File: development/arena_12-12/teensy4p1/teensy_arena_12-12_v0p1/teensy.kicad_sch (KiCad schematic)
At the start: 3 parts, among them J2 Conn_01x04, J3 Conn_01x04, U18 Teensy4.1

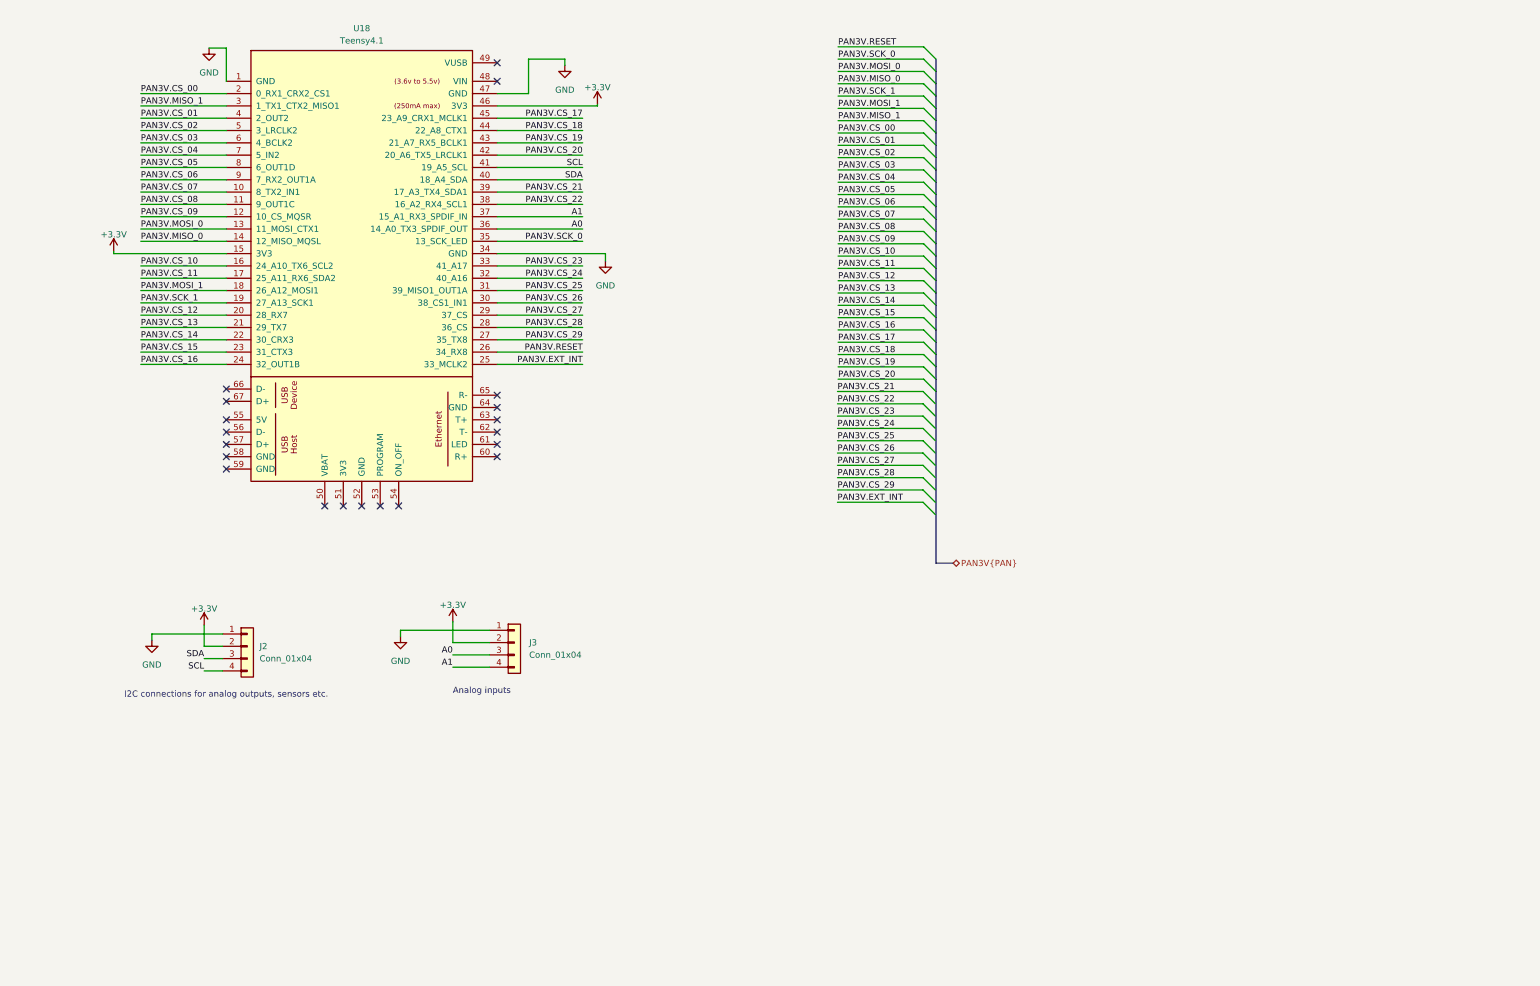
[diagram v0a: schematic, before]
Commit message: Worked on 12-12 teensy4p1 arena without vreg.
Modified SPI connections from teensy to panel columns so that all
signals go from a single source to a single destinatin. Also, added
source termination resistors and schmitt trigger buffers to all SPI
signals.
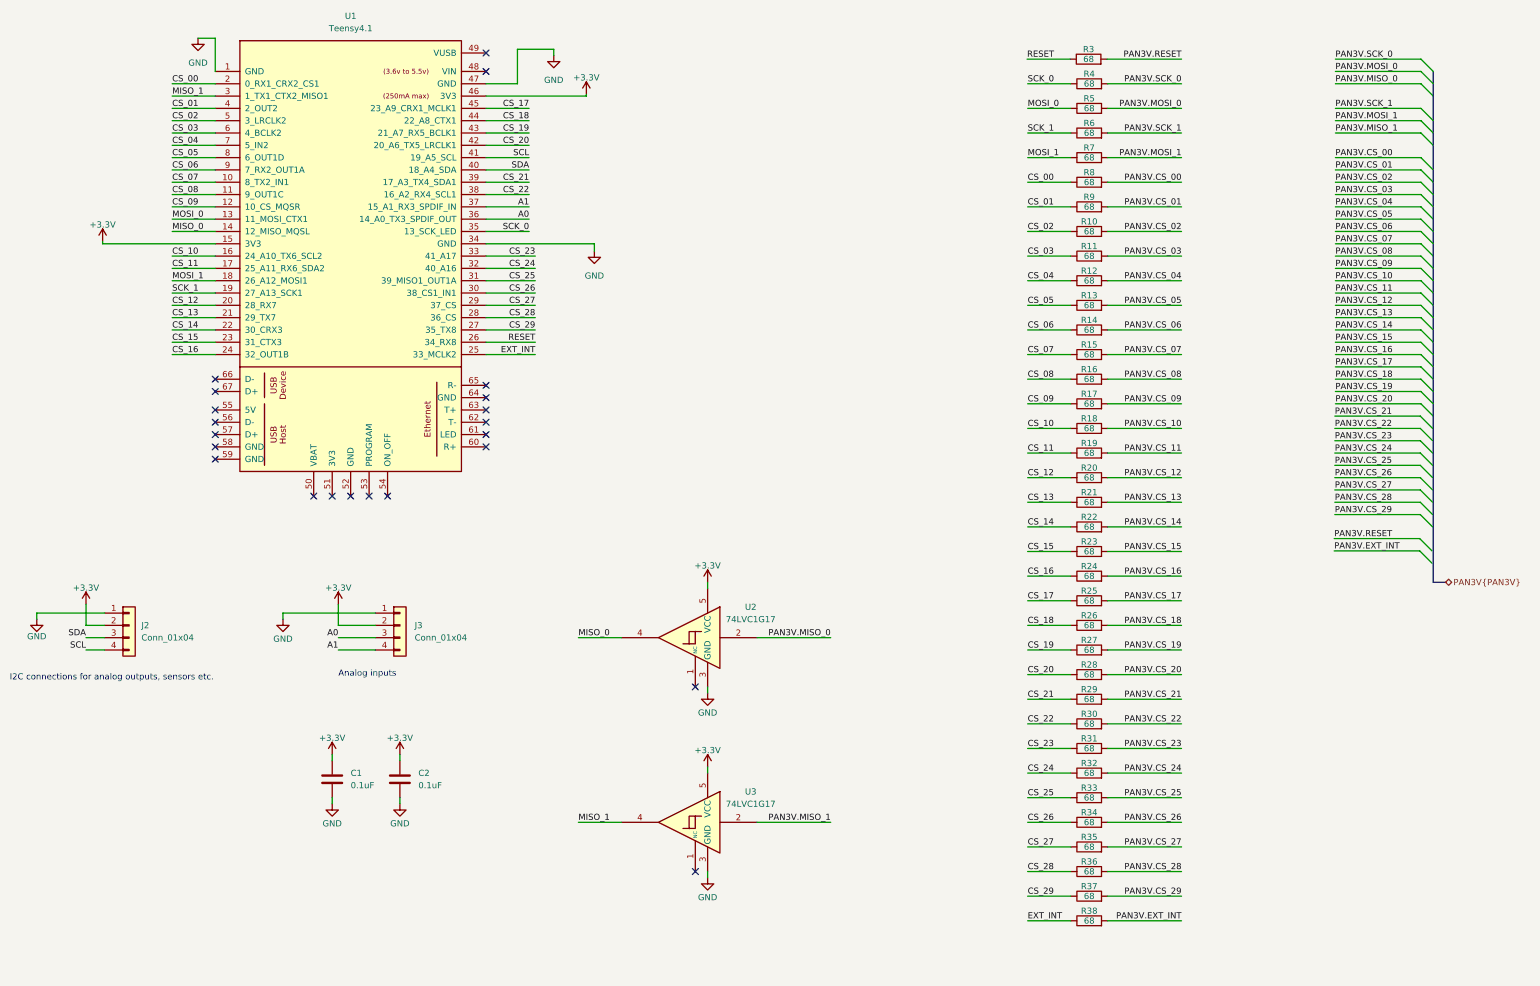
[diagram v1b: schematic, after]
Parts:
- added C1, C2: 0.1uF, symbol Device:C
- added R10, R11, R12, R13, R14, R15, R16, R17, R18, R19, R20, R21, R22, R23, R24, R25, R26, R27, R28, R29, R3, R30, R31, R32, R33, R34, R35, R36, R37, R38, R4, R5, R6, R7, R8, R9: 68, symbol Device:R
- added U2, U3: 74LVC1G17, symbol 74xGxx:74LVC1G17
- renumbered U18 to U1
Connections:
- net +3.3V: now also C1.1, C2.1, U2.5 (VCC), U3.5 (VCC)
- net GND: now also C1.2, C2.2, U2.3 (GND), U3.3 (GND)
- net PAN3V.CS_00: now also R8.2; no longer U1.2 (0_RX1_CRX2_CS1)
- net PAN3V.CS_01: now also R9.2; no longer U1.4 (2_OUT2)
- net PAN3V.CS_02: now also R10.2; no longer U1.5 (3_LRCLK2)
- net PAN3V.CS_03: now also R11.2; no longer U1.6 (4_BCLK2)
- net PAN3V.CS_04: now also R12.2; no longer U1.7 (5_IN2)
- net PAN3V.CS_05: now also R13.2; no longer U1.8 (6_OUT1D)
- net PAN3V.CS_06: now also R14.2; no longer U1.9 (7_RX2_OUT1A)
- net PAN3V.CS_07: now also R15.2; no longer U1.10 (8_TX2_IN1)
- net PAN3V.CS_08: now also R16.2; no longer U1.11 (9_OUT1C)
- net PAN3V.CS_09: now also R17.2; no longer U1.12 (10_CS_MQSR)
- net PAN3V.CS_10: now also R18.2; no longer U1.16 (24_A10_TX6_SCL2)
- net PAN3V.CS_11: now also R19.2; no longer U1.17 (25_A11_RX6_SDA2)
- net PAN3V.CS_12: now also R20.2; no longer U1.20 (28_RX7)
- net PAN3V.CS_13: now also R21.2; no longer U1.21 (29_TX7)
- net PAN3V.CS_14: now also R22.2; no longer U1.22 (30_CRX3)
- net PAN3V.CS_15: now also R23.2; no longer U1.23 (31_CTX3)
- net PAN3V.CS_16: now also R24.2; no longer U1.24 (32_OUT1B)
- net PAN3V.CS_17: now also R25.2; no longer U1.45 (23_A9_CRX1_MCLK1)
- net PAN3V.CS_18: now also R26.2; no longer U1.44 (22_A8_CTX1)
- net PAN3V.CS_19: now also R27.2; no longer U1.43 (21_A7_RX5_BCLK1)
- net PAN3V.CS_20: now also R28.2; no longer U1.42 (20_A6_TX5_LRCLK1)
- net PAN3V.CS_21: now also R29.2; no longer U1.39 (17_A3_TX4_SDA1)
- net PAN3V.CS_22: now also R30.2; no longer U1.38 (16_A2_RX4_SCL1)
- net PAN3V.CS_23: now also R31.2; no longer U1.33 (41_A17)
- net PAN3V.CS_24: now also R32.2; no longer U1.32 (40_A16)
- net PAN3V.CS_25: now also R33.2; no longer U1.31 (39_MISO1_OUT1A)
- net PAN3V.CS_26: now also R34.2; no longer U1.30 (38_CS1_IN1)
- net PAN3V.CS_27: now also R35.2; no longer U1.29 (37_CS)
- net PAN3V.CS_28: now also R36.2; no longer U1.28 (36_CS)
- net PAN3V.CS_29: now also R37.2; no longer U1.27 (35_TX8)
- net PAN3V.EXT_INT: now also R38.2; no longer U1.25 (33_MCLK2)
- net PAN3V.MISO_0: now also U2.2; no longer U1.14 (12_MISO_MQSL)
- net PAN3V.MISO_1: now also U3.2; no longer U1.3 (1_TX1_CTX2_MISO1)
- net PAN3V.MOSI_0: now also R5.2; no longer U1.13 (11_MOSI_CTX1)
- net PAN3V.MOSI_1: now also R7.2; no longer U1.18 (26_A12_MOSI1)
- net PAN3V.RESET: now also R3.2; no longer U1.26 (34_RX8)
- net PAN3V.SCK_0: now also R4.2; no longer U1.35 (13_SCK_LED)
- net PAN3V.SCK_1: now also R6.2; no longer U1.19 (27_A13_SCK1)
- new net CS_00: R8.1, U1.2 (0_RX1_CRX2_CS1)
- new net CS_01: R9.1, U1.4 (2_OUT2)
- new net CS_02: R10.1, U1.5 (3_LRCLK2)
- new net CS_03: R11.1, U1.6 (4_BCLK2)
- new net CS_04: R12.1, U1.7 (5_IN2)
- new net CS_05: R13.1, U1.8 (6_OUT1D)
- new net CS_06: R14.1, U1.9 (7_RX2_OUT1A)
- new net CS_07: R15.1, U1.10 (8_TX2_IN1)
- new net CS_08: R16.1, U1.11 (9_OUT1C)
- new net CS_09: R17.1, U1.12 (10_CS_MQSR)
- new net CS_10: R18.1, U1.16 (24_A10_TX6_SCL2)
- new net CS_11: R19.1, U1.17 (25_A11_RX6_SDA2)
- new net CS_12: R20.1, U1.20 (28_RX7)
- new net CS_13: R21.1, U1.21 (29_TX7)
- new net CS_14: R22.1, U1.22 (30_CRX3)
- new net CS_15: R23.1, U1.23 (31_CTX3)
- new net CS_16: R24.1, U1.24 (32_OUT1B)
- new net CS_17: R25.1, U1.45 (23_A9_CRX1_MCLK1)
- new net CS_18: R26.1, U1.44 (22_A8_CTX1)
- new net CS_19: R27.1, U1.43 (21_A7_RX5_BCLK1)
- new net CS_20: R28.1, U1.42 (20_A6_TX5_LRCLK1)
- new net CS_21: R29.1, U1.39 (17_A3_TX4_SDA1)
- new net CS_22: R30.1, U1.38 (16_A2_RX4_SCL1)
- new net CS_23: R31.1, U1.33 (41_A17)
- new net CS_24: R32.1, U1.32 (40_A16)
- new net CS_25: R33.1, U1.31 (39_MISO1_OUT1A)
- new net CS_26: R34.1, U1.30 (38_CS1_IN1)
- new net CS_27: R35.1, U1.29 (37_CS)
- new net CS_28: R36.1, U1.28 (36_CS)
- new net CS_29: R37.1, U1.27 (35_TX8)
- new net EXT_INT: R38.1, U1.25 (33_MCLK2)
- new net MISO_0: U1.14 (12_MISO_MQSL), U2.4
- new net MISO_1: U1.3 (1_TX1_CTX2_MISO1), U3.4
- new net MOSI_0: R5.1, U1.13 (11_MOSI_CTX1)
- new net MOSI_1: R7.1, U1.18 (26_A12_MOSI1)
- new net RESET: R3.1, U1.26 (34_RX8)
- new net SCK_0: R4.1, U1.35 (13_SCK_LED)
- new net SCK_1: R6.1, U1.19 (27_A13_SCK1)
- no-connect marks 20 -> 22
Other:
- moved on the sheet: J2, J3, U1

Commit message: More work on schematic for 12-12 teensy arena.
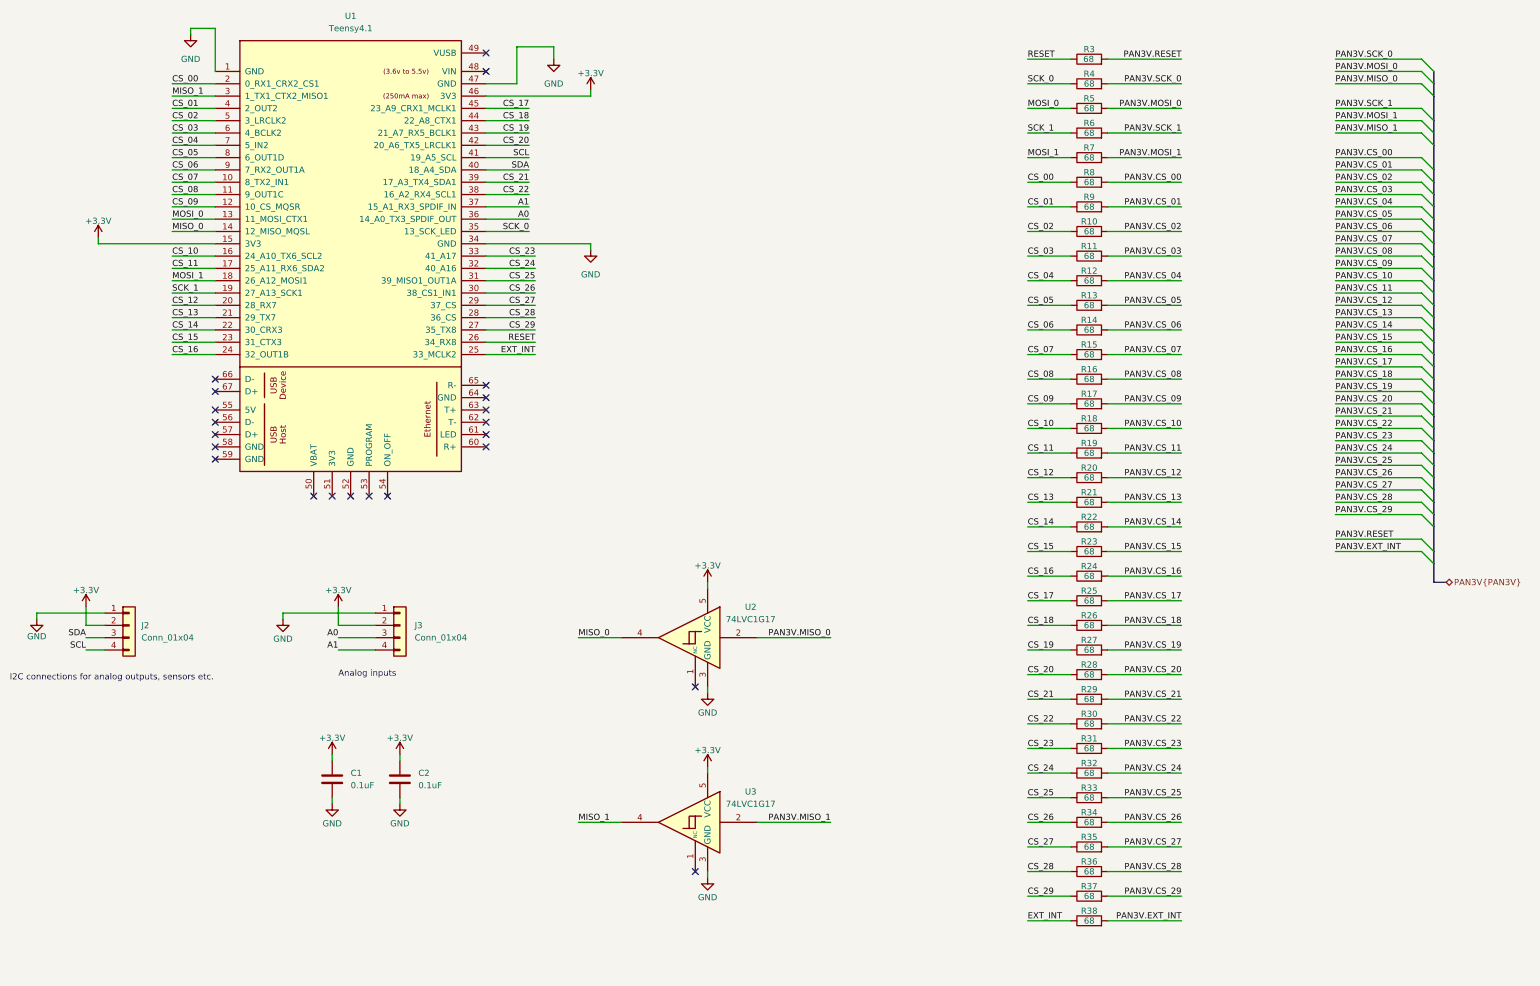
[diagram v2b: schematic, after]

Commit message: More work on schematic.
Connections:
- net CS_00 renamed TNY_CS_00
- net CS_01 renamed TNY_CS_01
- net CS_02 renamed TNY_CS_02
- net CS_03 renamed TNY_CS_03
- net CS_04 renamed TNY_CS_04
- net CS_05 renamed TNY_CS_05
- net CS_06 renamed TNY_CS_06
- net CS_07 renamed TNY_CS_07
- net CS_08 renamed TNY_CS_08
- net CS_09 renamed TNY_CS_09
- net CS_10 renamed TNY_CS_10
- net CS_11 renamed TNY_CS_11
- net CS_12 renamed TNY_CS_12
- net CS_13 renamed TNY_CS_13
- net CS_14 renamed TNY_CS_14
- net CS_15 renamed TNY_CS_15
- net CS_16 renamed TNY_CS_16
- net CS_17 renamed TNY_CS_17
- net CS_18 renamed TNY_CS_18
- net CS_19 renamed TNY_CS_19
- net CS_20 renamed TNY_CS_20
- net CS_21 renamed TNY_CS_21
- net CS_22 renamed TNY_CS_22
- net CS_23 renamed TNY_CS_23
- net CS_24 renamed TNY_CS_24
- net CS_25 renamed TNY_CS_25
- net CS_26 renamed TNY_CS_26
- net CS_27 renamed TNY_CS_27
- net CS_28 renamed TNY_CS_28
- net CS_29 renamed TNY_CS_29
- net EXT_INT renamed TNY_EXT_INT
- net MISO_0 renamed TNY_MISO_0
- net MISO_1 renamed TNY_MISO_1
- net MOSI_0 renamed TNY_MOSI_0
- net MOSI_1 renamed TNY_MOSI_1
- net RESET renamed TNY_RESET
- net SCK_0 renamed TNY_SCK_0
- net SCK_1 renamed TNY_SCK_1
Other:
- moved on the sheet: R3, R38, R4, R5, R6, R7

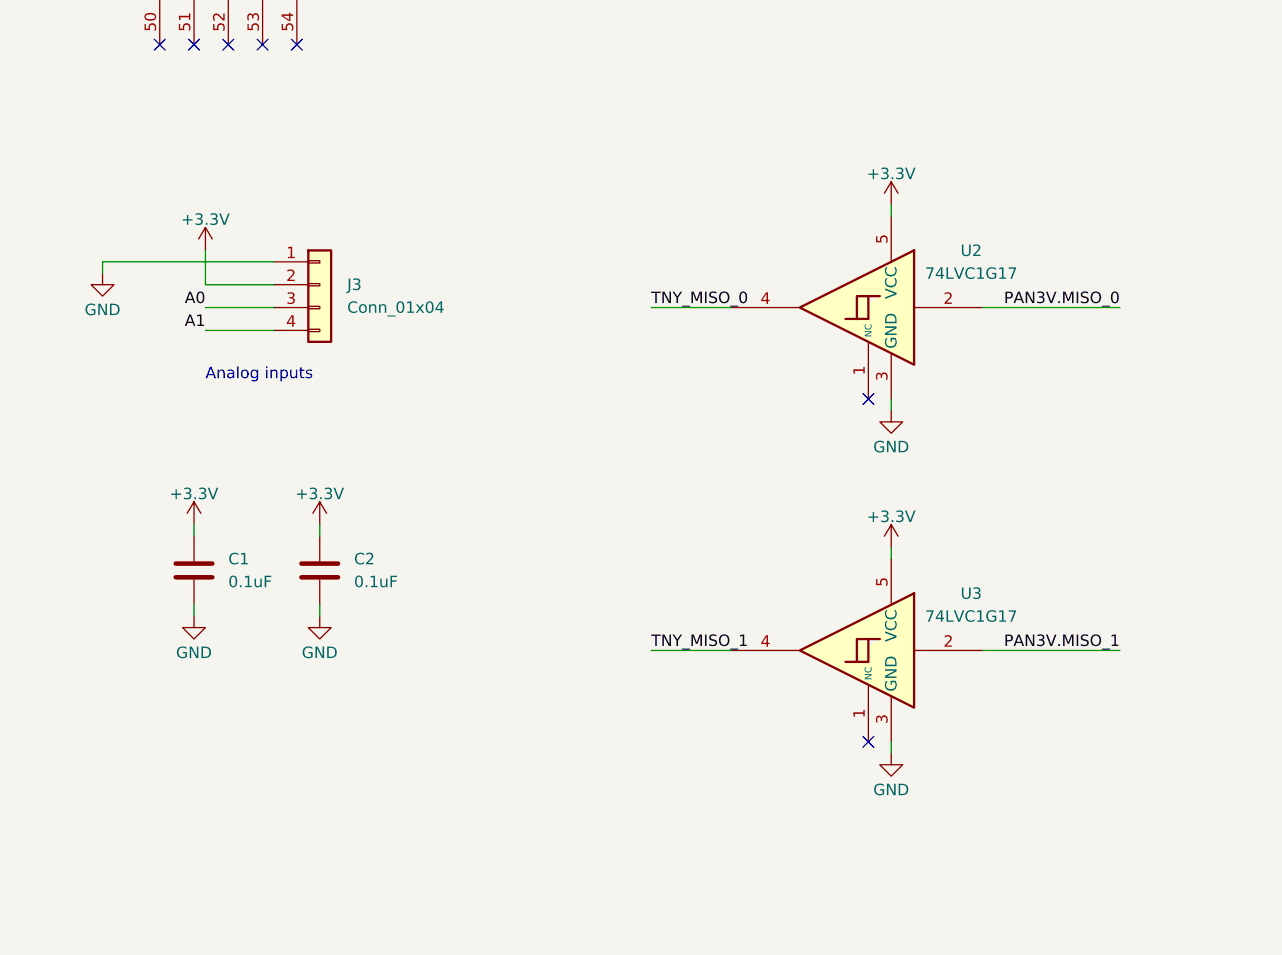
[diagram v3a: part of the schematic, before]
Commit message: Reworked schematic for 12-12 teensy arena w/o regulators some more.
Worked on foot print assignmets. Started replacing some of the single
schmitt triggers with equivalent dual versions to reduce component
count.
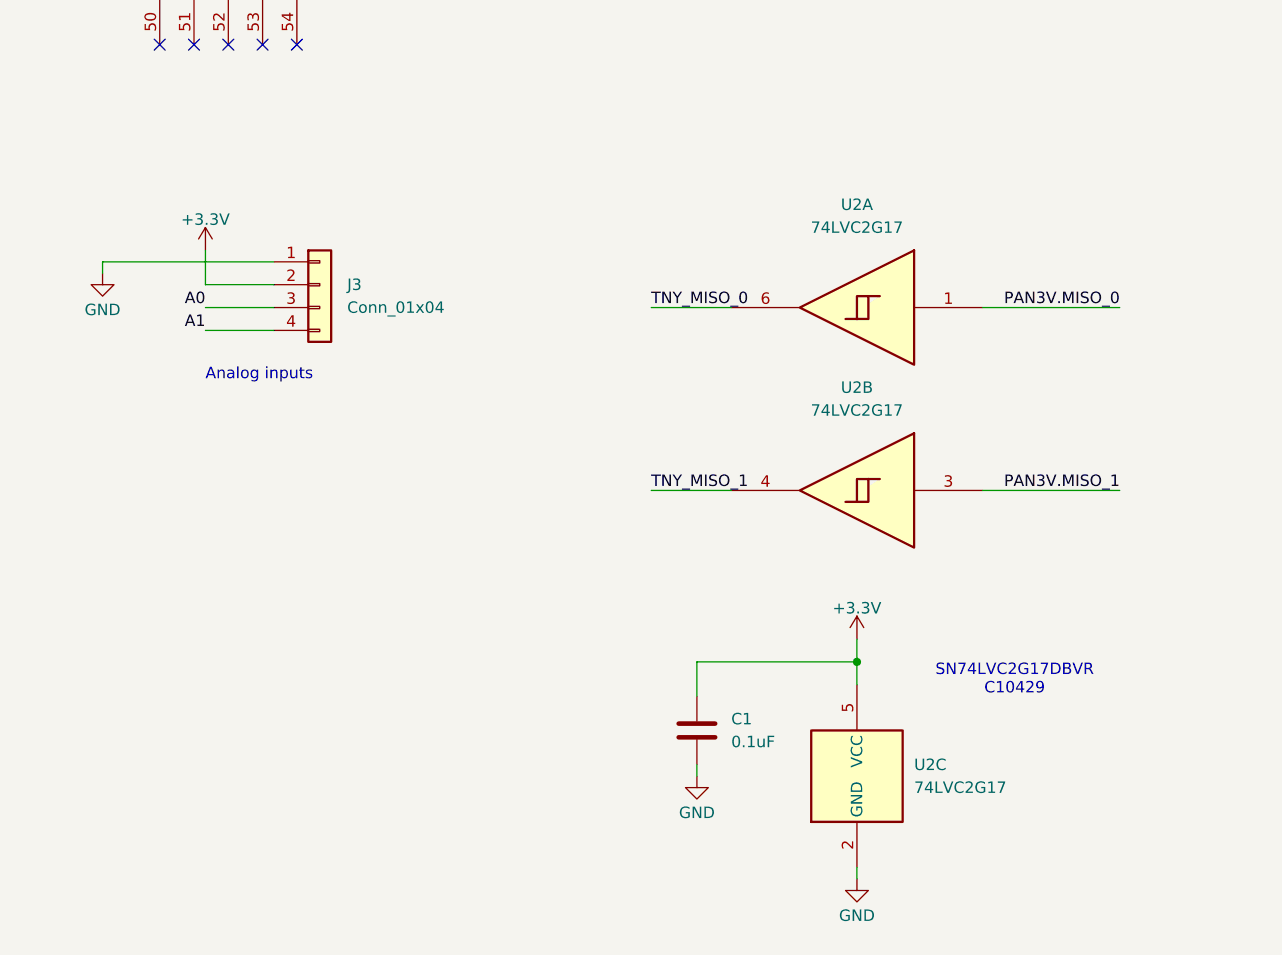
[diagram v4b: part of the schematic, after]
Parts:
- removed C2: 0.1uF, symbol Device:C
- removed U2, U3: 74LVC1G17, symbol 74xGxx:74LVC1G17
- added U2: 74LVC2G17, symbol 74xGxx:74LVC2G17
- C1: footprint (none) -> Capacitor_SMD:C_0603_1608Metric
- R10, R11, R12, R13, R14, R15, R16, R17, R18, R19, R20, R21, R22, R23, R24, R25, R26, R27, R28, R29, R3, R30, R31, R32, R33, R34, R35, R36, R37, R38, R4, R5, R6, R7, R8, R9: footprint (none) -> Resistor_SMD:R_0603_1608Metric
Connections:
- net +3.3V: now also U2.5 (VCC)
- net GND: now also U2.2 (GND)
- net PAN3V.MISO_0: now also U2.1
- net PAN3V.MISO_1: now also U2.3
- net TNY_MISO_0: now also U2.6
- net TNY_MISO_1: now also U2.4
- no-connect marks 22 -> 20
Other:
- note added: "SN74LVC2G17DBVR C10429"
- moved on the sheet: C1

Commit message: Finished initial schematic for 12-12 teensy 4.1 arena w/o vreg.
Finished footprint assignments and started working on layout changes.
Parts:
- U2: footprint (none) -> Package_TO_SOT_SMD:SOT-23-6
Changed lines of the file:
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@@
 			)
 		)
-		(property "Footprint" ""
+		(property "Footprint" "Package_TO_SOT_SMD:SOT-23-6"
 			(at 171.45 168.91 0)
 			(effects
@@
 			)
 		)
-		(property "Footprint" ""
+		(property "Footprint" "Package_TO_SOT_SMD:SOT-23-6"
 			(at 172.72 200.66 0)
 			(effects
@@
 			)
 		)
-		(property "Footprint" ""
+		(property "Footprint" "Package_TO_SOT_SMD:SOT-23-6"
 			(at 171.45 148.59 0)
 			(effects
